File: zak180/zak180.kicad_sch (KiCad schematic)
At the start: 0 parts

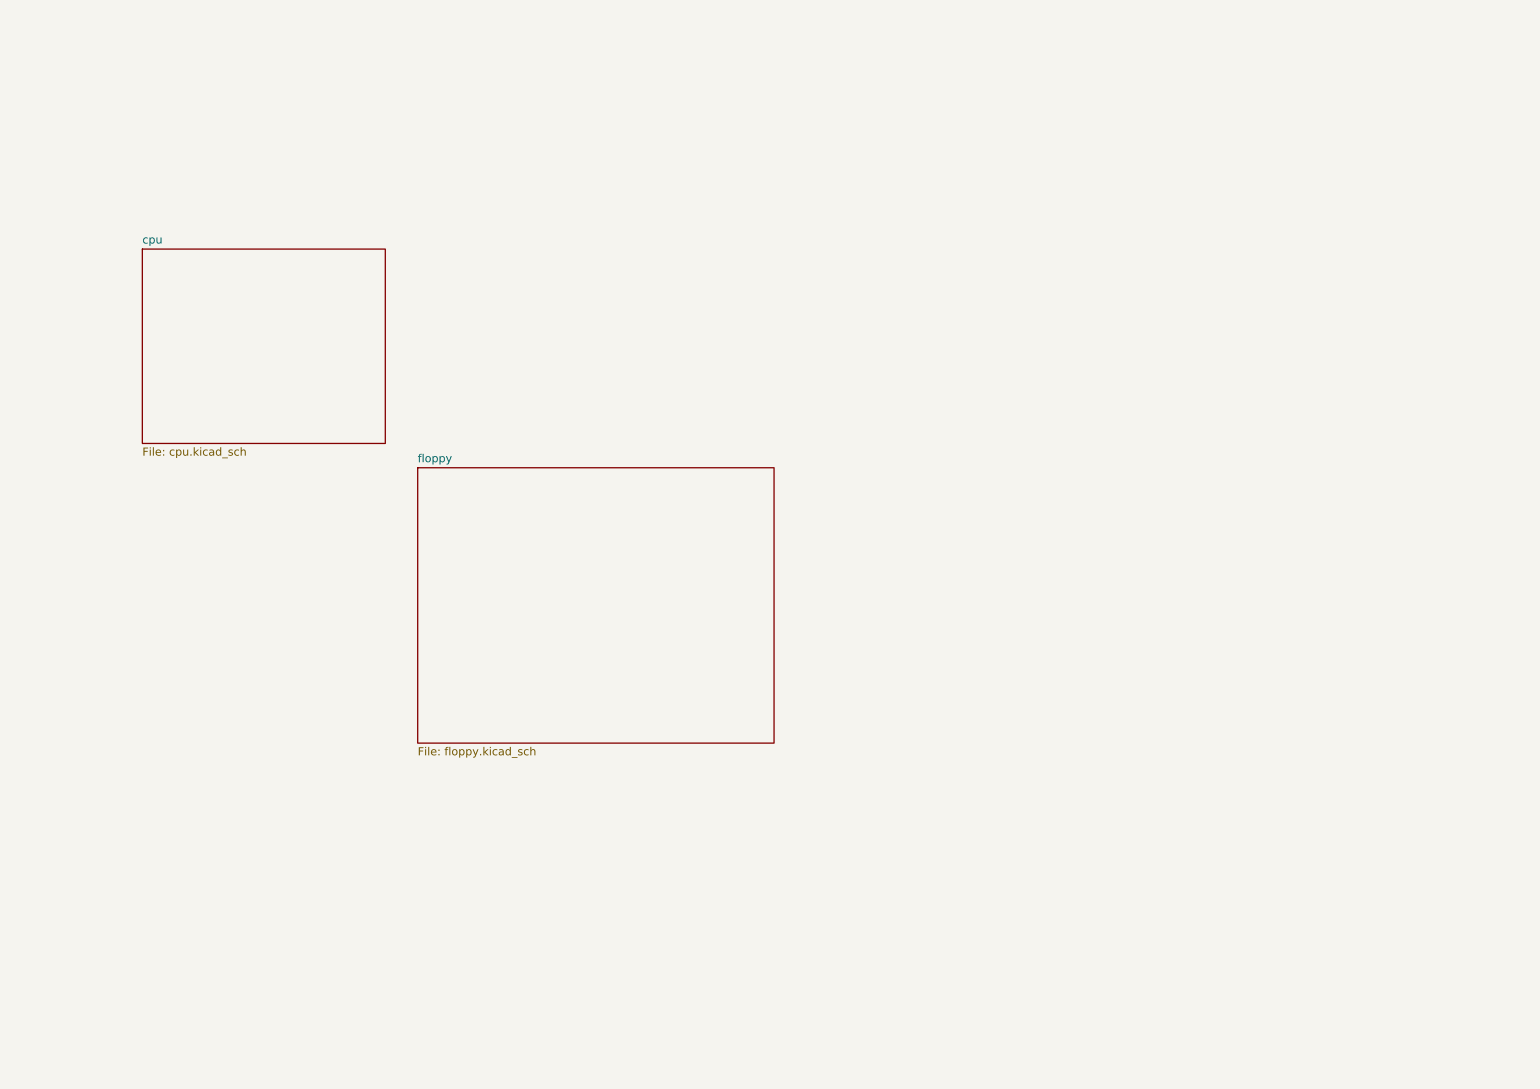
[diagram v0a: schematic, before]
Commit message: HW: Floppy, VGA, PIO and sound
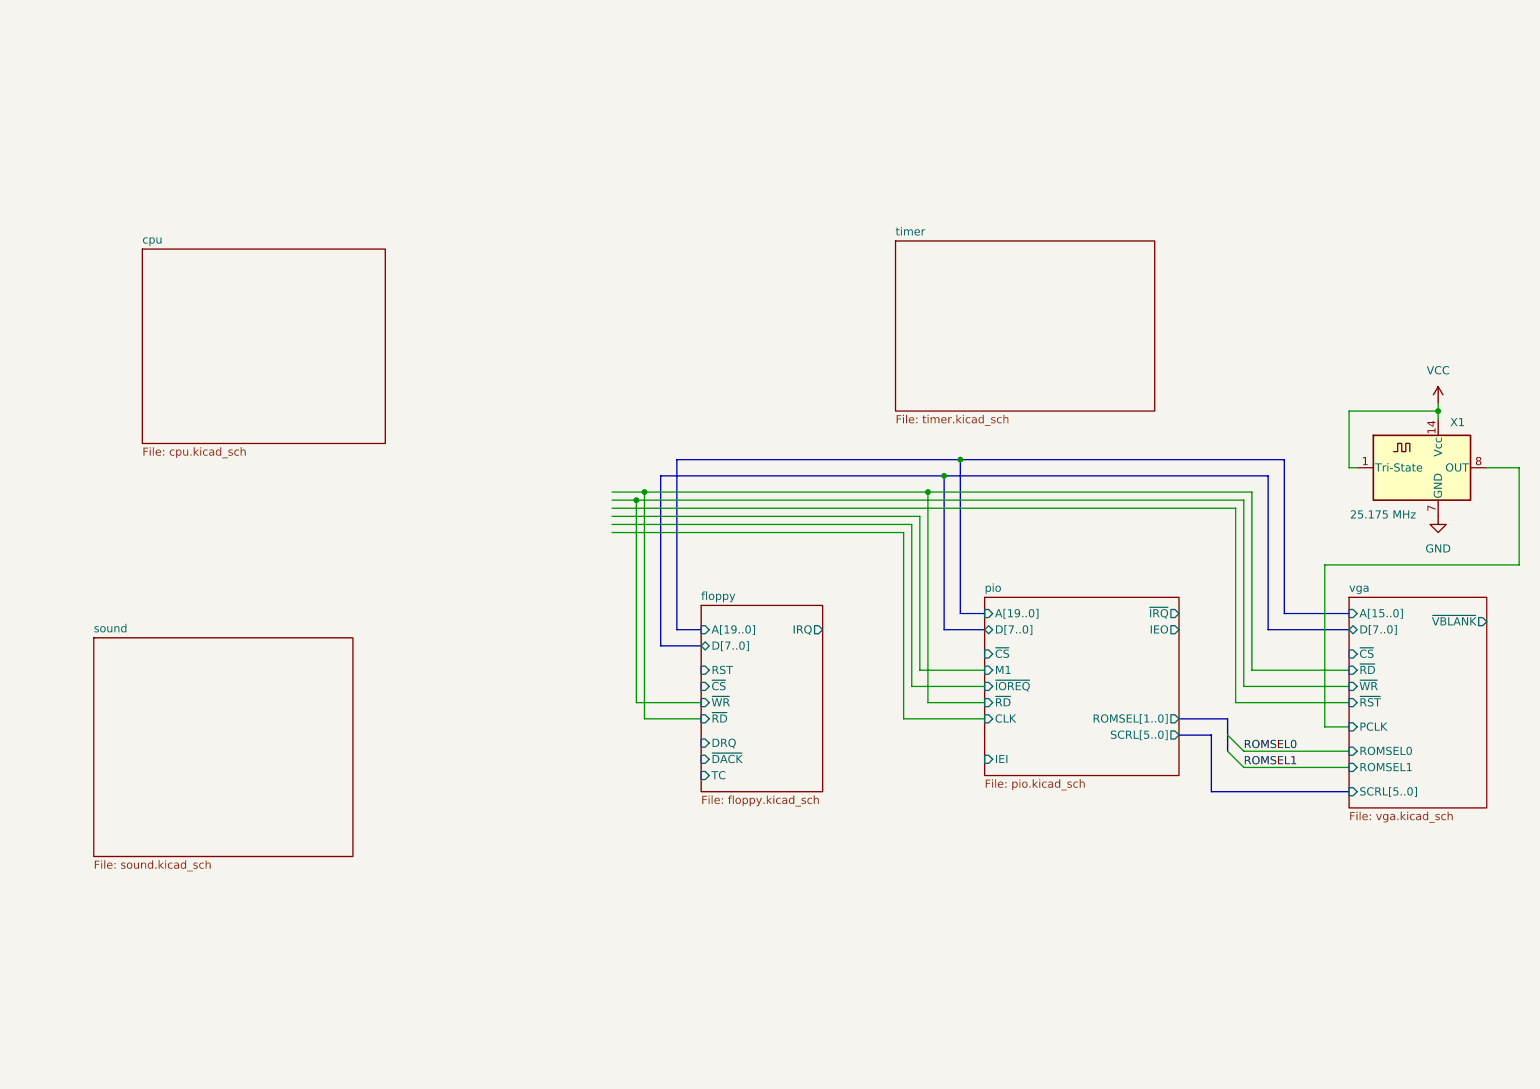
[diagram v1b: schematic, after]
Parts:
- added X1: 25.175 MHz, Oscillator:Oscillator_DIP-14, symbol Oscillator:ACO-xxxMHz-A
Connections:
- new net GND: X1.7 (GND)
- new net VCC: X1.1 (Tri-State), X1.14 (Vcc)
- new net vga/PCLK: X1.8 (OUT)
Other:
- added sheet pio (pio.kicad_sch)
- added sheet sound (sound.kicad_sch)
- added sheet timer (timer.kicad_sch)
- added sheet vga (vga.kicad_sch)
- sheet floppy ports: added A[19..0], DRQ, D[7..0], IRQ, RST, TC, ~{CS}, ~{DACK}, ~{RD}, ~{WR}; removed none

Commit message: HW: Further work on schematic
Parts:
- removed X1: 25.175 MHz, Oscillator:Oscillator_DIP-14, symbol Oscillator:ACO-xxxMHz-A
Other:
- removed sheet timer
- added sheet clock (clock.kicad_sch)
- added sheet keyboard (keyboard.kicad_sch)
- sheet cpu ports: added A[19..0], CLK, D[7..0], RX0, RX1, TX0, TX1, ~{BUSACK}, ~{BUSREQ}, ~{DREQ0}, ~{DREQ1}, ~{FLOPPY}, ~{HALT}, ~{INT0}, ~{INT1}, ~{INT2}, ~{IORQ}, ~{KEYBOARD}, ~{M1}, ~{NMI}, ~{PIO}, ~{RAM}, ~{RD}, ~{RFSH}, ~{ROM}, ~{RST}, ~{SOUND}, ~{TEND0}, ~{TEND1}, ~{VRAM}, ~{WAIT}, ~{WR}; removed none
- sheet floppy ports: added A[2..0]; removed A[19..0]
- sheet pio ports: added A[1..0]; removed A[19..0], ROMSEL[1..0], SCRL[5..0]
- sheet sound ports: added A0, CLK, D[7..0], ROMSEL[1..0], SCRL[5..0], ~{CS}, ~{RD}, ~{RST}, ~{WR}; removed none
- sheet vga ports: added A[12..0], ROMSEL[1..0], VBLANK; removed A[15..0], ROMSEL0, ROMSEL1, ~{VBLANK}

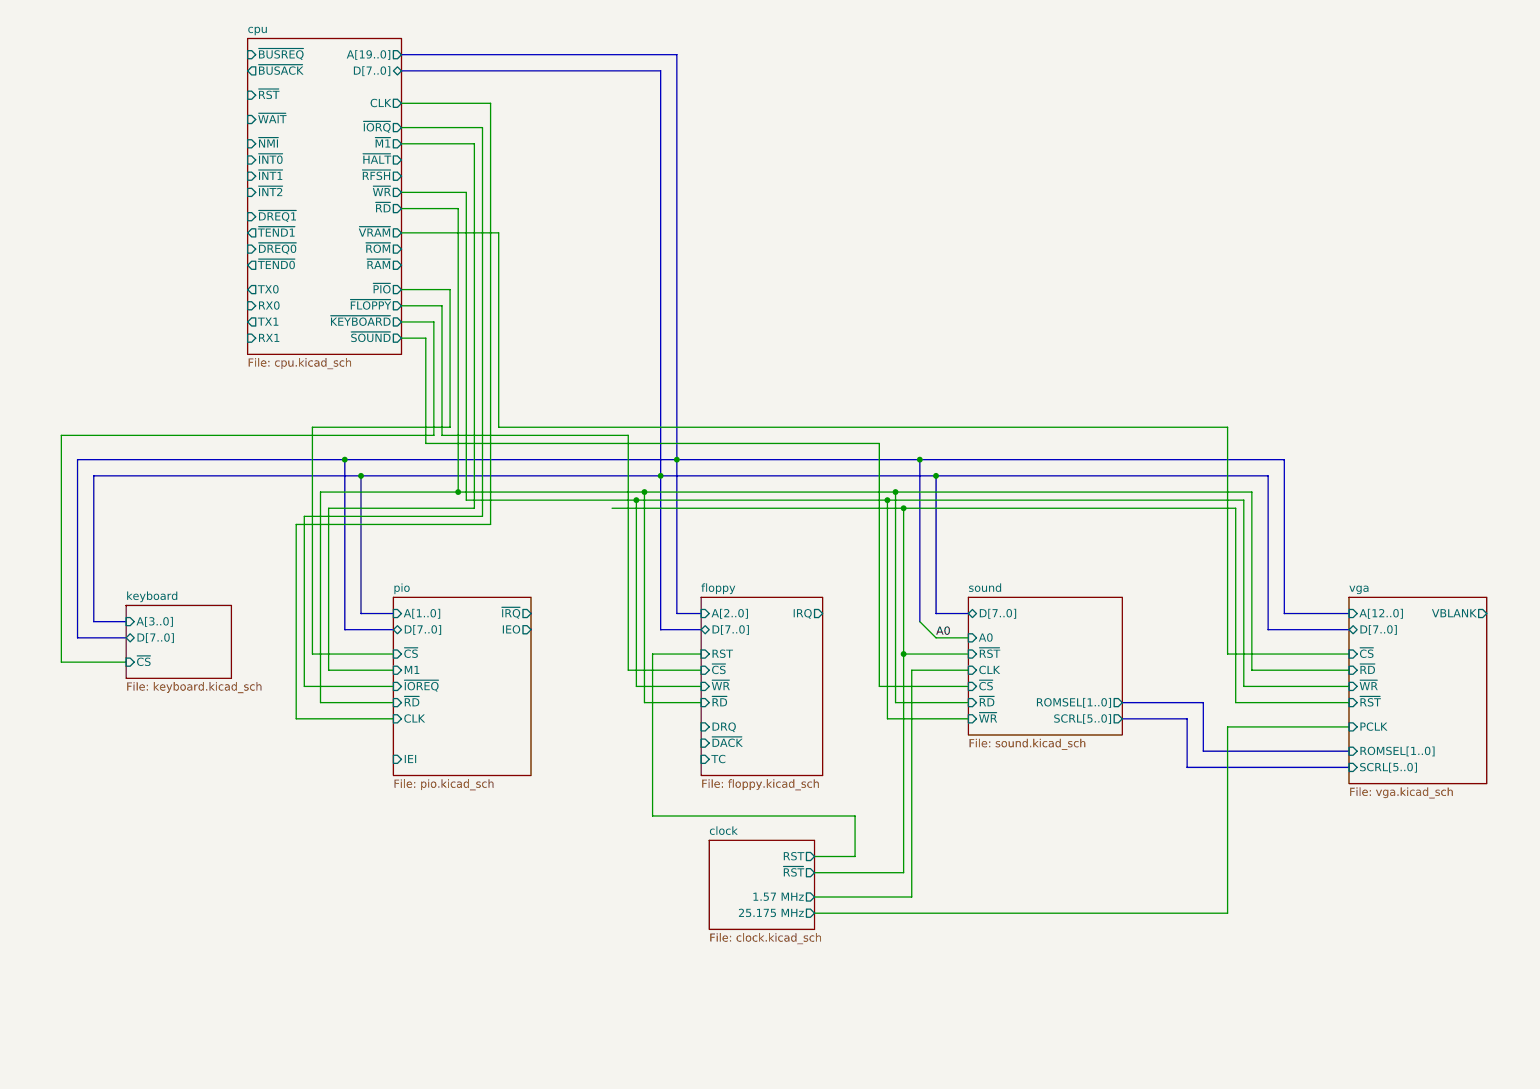
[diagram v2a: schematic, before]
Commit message: HW: Add memory, serial and power
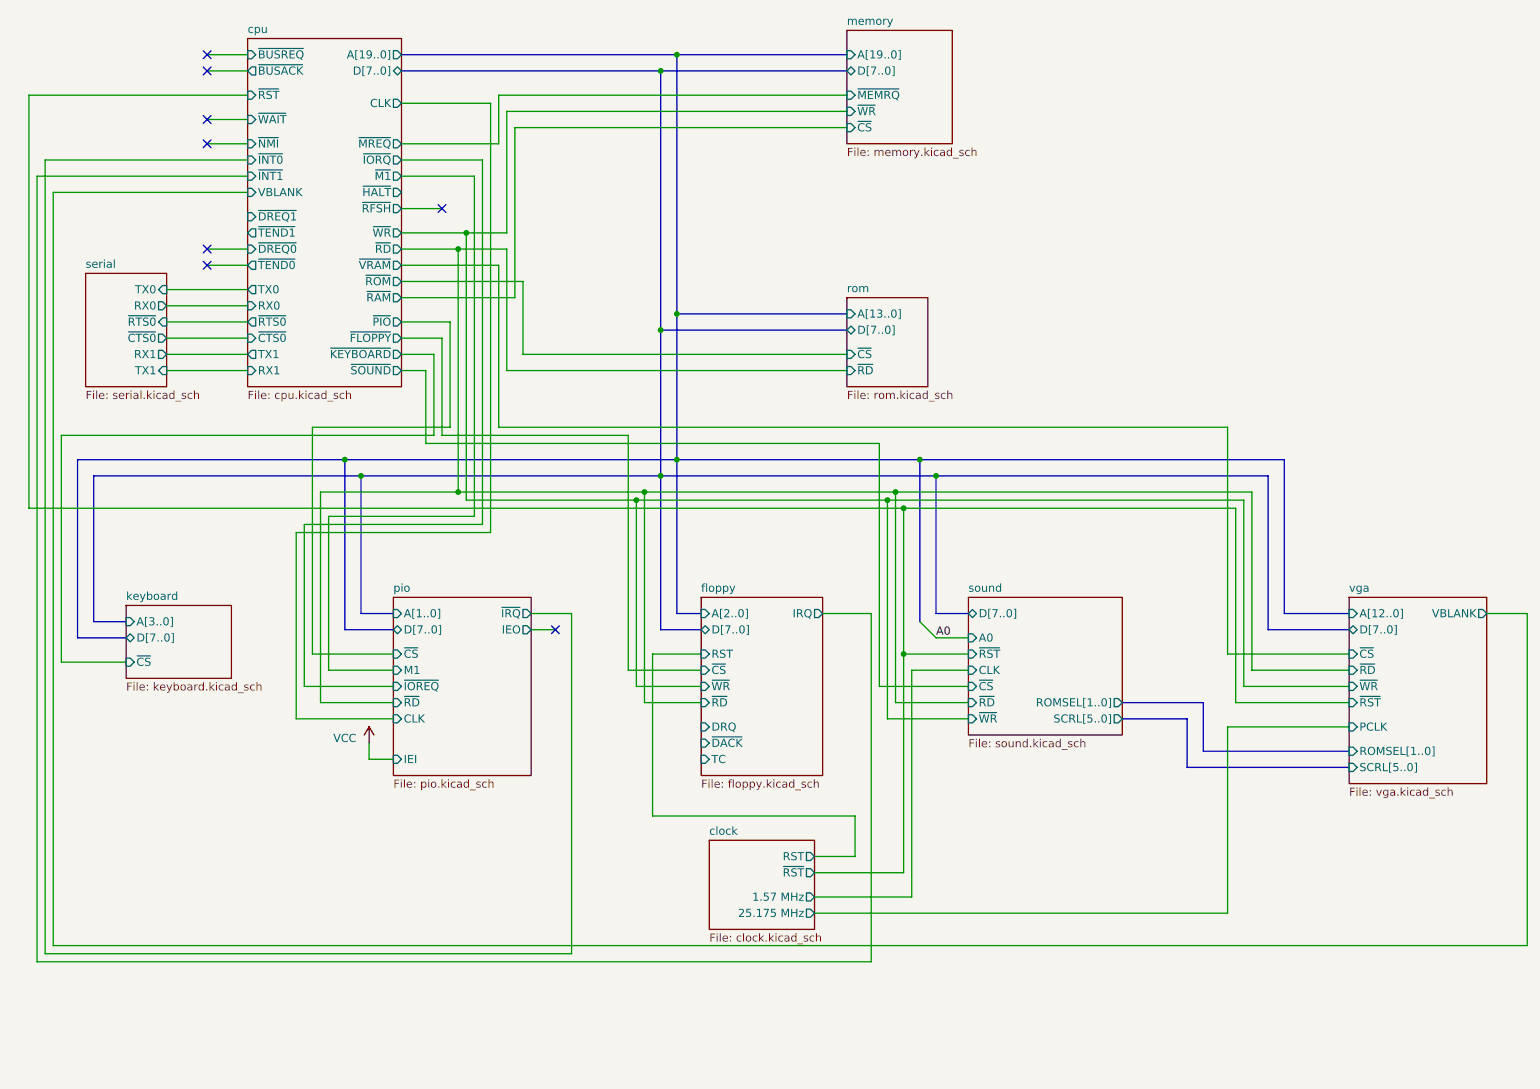
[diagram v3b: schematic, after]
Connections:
- no-connect marks 0 -> 8
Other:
- added sheet memory (memory.kicad_sch)
- added sheet rom (rom.kicad_sch)
- added sheet serial (serial.kicad_sch)
- sheet cpu ports: added VBLANK, ~{CTS0}, ~{MREQ}, ~{RTS0}; removed ~{INT2}

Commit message: HW: Before abandoning DRAM
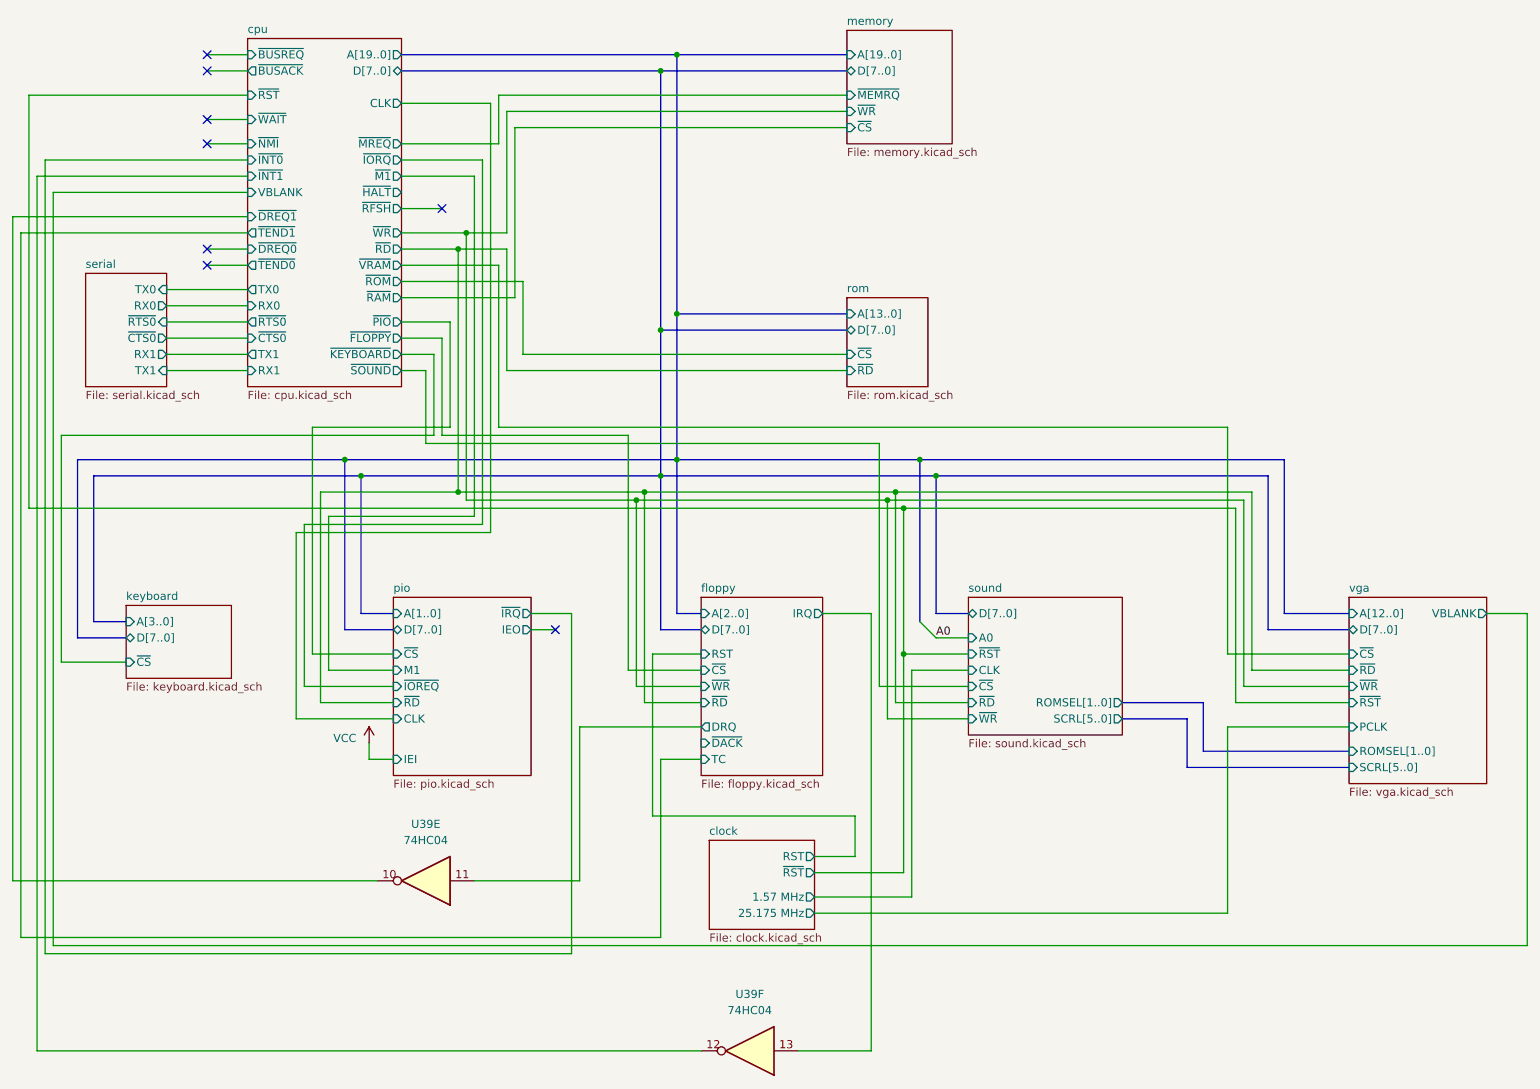
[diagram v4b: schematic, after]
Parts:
- added U39: 74HC04, symbol 74xx:74HC04
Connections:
- net cpu/~{DREQ1}: now also U39.10
- net cpu/~{INT1}: now also U39.12
- net floppy/DRQ: now also U39.11
- new net floppy/IRQ: U39.13
